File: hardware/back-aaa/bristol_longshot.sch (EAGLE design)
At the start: 7 parts, among them U4 ADP1607ACPZN-R7

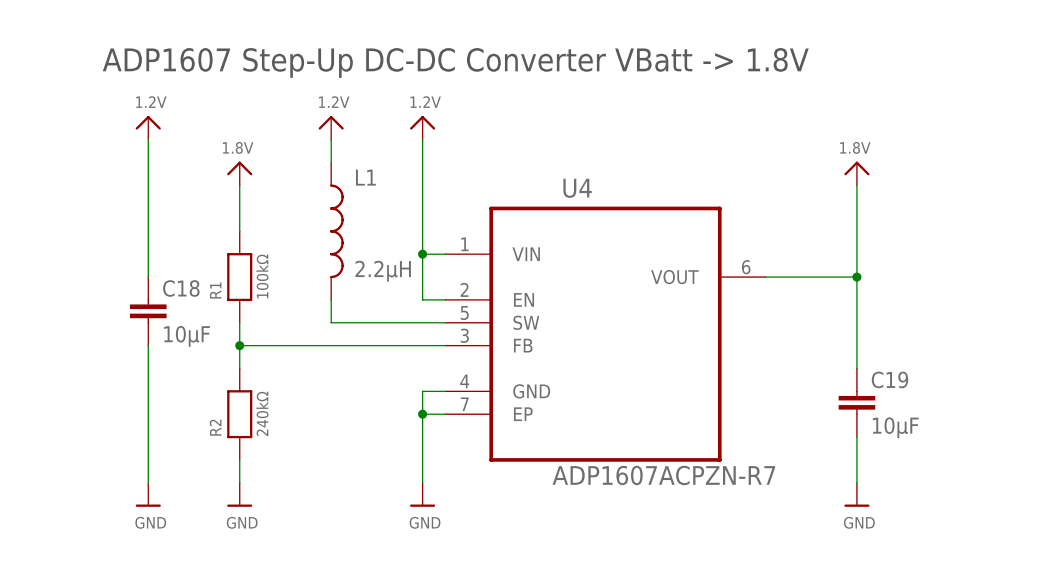
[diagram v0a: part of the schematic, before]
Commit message: Added partslist, updated parts for back-aaa
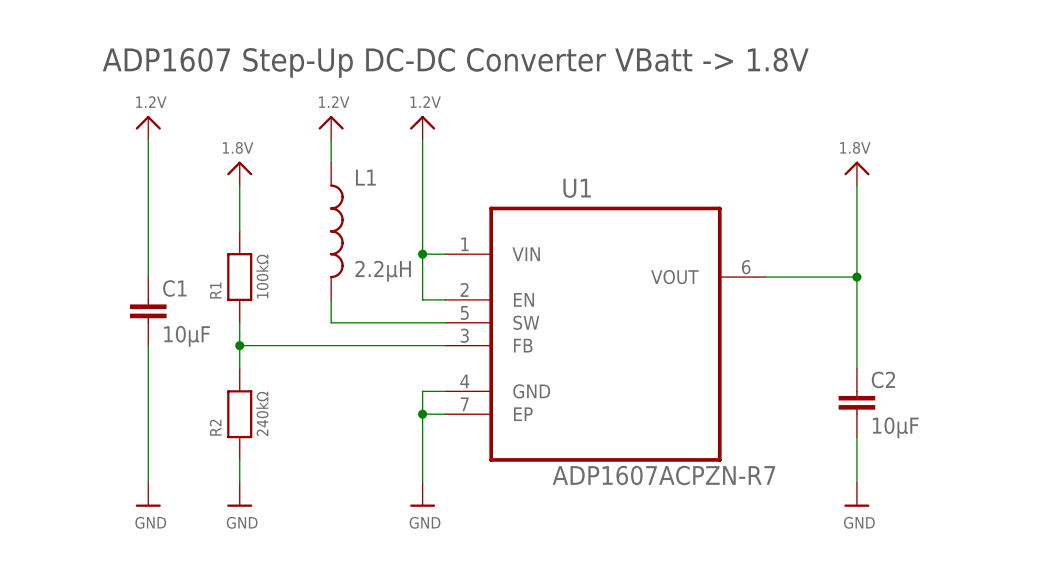
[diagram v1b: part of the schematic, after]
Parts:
- renumbered C18 to C1, C19 to C2, U4 to U1
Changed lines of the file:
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@@
 <part name="U$47" library="microbuilder_v3" deviceset="1.2V" device=""/>
 <part name="U$2" library="fbri" deviceset="AA_HOLDER" device=""/>
-<part name="C19" library="resistor" deviceset="C-EU" device="C0603K" value="10µF"/>
-<part name="U4" library="ADP1607" deviceset="ADP1607ACPZN-R7" device=""/>
+<part name="C2" library="resistor" deviceset="C-EU" device="C0603K" value="10µF"/>
+<part name="U1" library="ADP1607" deviceset="ADP1607ACPZN-R7" device=""/>
 <part name="U$26" library="microbuilder_v3" deviceset="1.2V" device=""/>
 <part name="R1" library="microbuilder_v3" deviceset="RESISTOR" device="_0402" value="100kΩ"/>
@@
 <part name="U$35" library="microbuilder_v3" deviceset="1.2V" device=""/>
 <part name="U$36" library="microbuilder_v3" deviceset="GND" device=""/>
-<part name="C18" library="resistor" deviceset="C-EU" device="C0603K" value="10µF"/>
+<part name="C1" library="resistor" deviceset="C-EU" device="C0603K" value="10µF"/>
 <part name="U$52" library="microbuilder_v3" deviceset="1.8V" device=""/>
 </parts>
@@
 <instance part="U$47" gate="G$1" x="60.96" y="106.68"/>
 <instance part="U$2" gate="G$1" x="60.96" y="86.36" rot="R270"/>
-<instance part="C19" gate="G$1" x="170.18" y="83.82"/>
-<instance part="U4" gate="A" x="142.24" y="93.98"/>
+<instance part="C2" gate="G$1" x="170.18" y="83.82"/>
+<instance part="U1" gate="A" x="142.24" y="93.98"/>
 <instance part="U$26" gate="G$1" x="111.76" y="114.3"/>
 <instance part="R1" gate="G$1" x="101.6" y="96.52" rot="R90"/>
@@
 <instance part="U$35" gate="G$1" x="91.44" y="114.3"/>
 <instance part="U$36" gate="G$1" x="91.44" y="71.12"/>
-<instance part="C18" gate="G$1" x="91.44" y="93.98"/>
+<instance part="C1" gate="G$1" x="91.44" y="93.98"/>
 <instance part="U$52" gate="G$1" x="101.6" y="109.22" rot="MR0"/>
 </instances>
@@
 <segment>
 <pinref part="U$29" gate="G$1" pin="GND"/>
-<pinref part="C19" gate="G$1" pin="2"/>
+<pinref part="C2" gate="G$1" pin="2"/>
 <wire x1="170.18" y1="73.66" x2="170.18" y2="78.74" width="0.1524" layer="91"/>
 </segment>
@@
 </segment>
 <segment>
-<pinref part="U4" gate="A" pin="GND"/>
+<pinref part="U1" gate="A" pin="GND"/>
 <pinref part="U$1" gate="G$1" pin="GND"/>
 <wire x1="124.46" y1="83.82" x2="121.92" y2="83.82" width="0.1524" layer="91"/>
 <wire x1="121.92" y1="83.82" x2="121.92" y2="81.28" width="0.1524" layer="91"/>
-<pinref part="U4" gate="A" pin="EP"/>
+<pinref part="U1" gate="A" pin="EP"/>
 <wire x1="121.92" y1="81.28" x2="121.92" y2="73.66" width="0.1524" layer="91"/>
 <wire x1="124.46" y1="81.28" x2="121.92" y2="81.28" width="0.1524" layer="91"/>
@@
 <segment>
 <pinref part="U$36" gate="G$1" pin="GND"/>
-<pinref part="C18" gate="G$1" pin="2"/>
+<pinref part="C1" gate="G$1" pin="2"/>
 <wire x1="91.44" y1="73.66" x2="91.44" y2="88.9" width="0.1524" layer="91"/>
 </segment>
@@
 <pinref part="U$30" gate="G$1" pin="1.8V"/>
 <wire x1="170.18" y1="86.36" x2="170.18" y2="96.52" width="0.1524" layer="91"/>
-<pinref part="C19" gate="G$1" pin="1"/>
-<pinref part="U4" gate="A" pin="VOUT"/>
+<pinref part="C2" gate="G$1" pin="1"/>
+<pinref part="U1" gate="A" pin="VOUT"/>
 <wire x1="170.18" y1="96.52" x2="170.18" y2="106.68" width="0.1524" layer="91"/>
 <wire x1="160.02" y1="96.52" x2="170.18" y2="96.52" width="0.1524" layer="91"/>
@@
 </segment>
 <segment>
-<pinref part="U4" gate="A" pin="VIN"/>
+<pinref part="U1" gate="A" pin="VIN"/>
 <pinref part="U$33" gate="G$1" pin="1.2V"/>
 <wire x1="124.46" y1="99.06" x2="121.92" y2="99.06" width="0.1524" layer="91"/>
 <wire x1="121.92" y1="99.06" x2="121.92" y2="111.76" width="0.1524" layer="91"/>
-<pinref part="U4" gate="A" pin="EN"/>
+<pinref part="U1" gate="A" pin="EN"/>
 <wire x1="124.46" y1="93.98" x2="121.92" y2="93.98" width="0.1524" layer="91"/>
 <wire x1="121.92" y1="93.98" x2="121.92" y2="99.06" width="0.1524" layer="91"/>
@@
 <pinref part="U$35" gate="G$1" pin="1.2V"/>
 <wire x1="91.44" y1="96.52" x2="91.44" y2="111.76" width="0.1524" layer="91"/>
-<pinref part="C18" gate="G$1" pin="1"/>
+<pinref part="C1" gate="G$1" pin="1"/>
 </segment>
 </net>
 <net name="SW" class="0">
 <segment>
-<pinref part="U4" gate="A" pin="SW"/>
+<pinref part="U1" gate="A" pin="SW"/>
 <wire x1="124.46" y1="91.44" x2="111.76" y2="91.44" width="0.1524" layer="91"/>
 <pinref part="L1" gate="G$1" pin="2"/>
@@
 <net name="FB" class="0">
 <segment>
-<pinref part="U4" gate="A" pin="FB"/>
+<pinref part="U1" gate="A" pin="FB"/>
 <pinref part="R2" gate="G$1" pin="2"/>
 <wire x1="124.46" y1="88.9" x2="101.6" y2="88.9" width="0.1524" layer="91"/>

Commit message: aaa-board mostly done
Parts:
- added C3: 100pF, microbuilder_v3:CAP_CERAMIC_0402
- added U$12: M04X2, fbri:M04X2
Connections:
- net 1.2V: now also U$12.5, U$2.+2; no longer U$2.+
- net 1.8V: now also C3.P$1, U$12.3
- net GND: now also C3.P$2, U$12.1, U$12.2, U$12.4, U$12.6
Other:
- note added: "GND, GND, 1.8V, Vbattery, DATA"
- note added: "NC, GND, Status, Vsolar, CLK"
- moved on the sheet: C2
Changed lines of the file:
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@@
 <part name="C1" library="resistor" deviceset="C-EU" device="C0603K" value="10µF"/>
 <part name="U$52" library="microbuilder_v3" deviceset="1.8V" device=""/>
+<part name="C3" library="microbuilder_v3" deviceset="CAP_CERAMIC" device="_0402" value="100pF"/>
+<part name="U$3" library="microbuilder_v3" deviceset="GND" device=""/>
+<part name="U$10" library="microbuilder_v3" deviceset="1.8V" device=""/>
+<part name="U$11" library="microbuilder_v3" deviceset="1.2V" device=""/>
+<part name="U$12" library="fbri" deviceset="M04X2" device=""/>
+<part name="U$6" library="microbuilder_v3" deviceset="GND" device=""/>
+<part name="U$13" library="microbuilder_v3" deviceset="GND" device=""/>
+<part name="U$14" library="microbuilder_v3" deviceset="GND" device=""/>
+<part name="U$15" library="microbuilder_v3" deviceset="GND" device=""/>
 </parts>
 <sheets>
@@
 connection on the
 holder</text>
+<text x="33.02" y="43.18" size="1.27" layer="97" font="vector" ratio="11">NC, GND, Status, Vsolar, CLK</text>
+<text x="33.02" y="5.08" size="1.27" layer="97" font="vector" ratio="11">GND, GND, 1.8V, Vbattery, DATA</text>
 </plain>
 <instances>
@@
 <instance part="FRAME1" gate="G$2" x="147.32" y="0"/>
 <instance part="U$1" gate="G$1" x="121.92" y="71.12"/>
-<instance part="U$29" gate="G$1" x="170.18" y="71.12"/>
-<instance part="U$30" gate="G$1" x="170.18" y="109.22" rot="MR0"/>
+<instance part="U$29" gate="G$1" x="185.42" y="71.12"/>
+<instance part="U$30" gate="G$1" x="185.42" y="109.22" rot="MR0"/>
 <instance part="L1" gate="G$1" x="111.76" y="101.6"/>
 <instance part="U$33" gate="G$1" x="121.92" y="114.3"/>
 <instance part="U$46" gate="G$1" x="60.96" y="71.12"/>
-<instance part="U$47" gate="G$1" x="60.96" y="106.68"/>
+<instance part="U$47" gate="G$1" x="63.5" y="106.68"/>
 <instance part="U$2" gate="G$1" x="60.96" y="86.36" rot="R270"/>
-<instance part="C2" gate="G$1" x="170.18" y="83.82"/>
+<instance part="C2" gate="G$1" x="185.42" y="83.82"/>
 <instance part="U1" gate="A" x="142.24" y="93.98"/>
 <instance part="U$26" gate="G$1" x="111.76" y="114.3"/>
@@
 <instance part="C1" gate="G$1" x="91.44" y="93.98"/>
 <instance part="U$52" gate="G$1" x="101.6" y="109.22" rot="MR0"/>
+<instance part="C3" gate="G$1" x="172.72" y="81.28"/>
+<instance part="U$3" gate="G$1" x="172.72" y="71.12"/>
+<instance part="U$10" gate="G$1" x="45.72" y="12.7" rot="MR180"/>
+<instance part="U$11" gate="G$1" x="48.26" y="12.7" rot="R180"/>
+<instance part="U$12" gate="G$1" x="48.26" y="27.94" rot="R90"/>
+<instance part="U$6" gate="G$1" x="43.18" y="17.78"/>
+<instance part="U$13" gate="G$1" x="43.18" y="38.1" rot="R180"/>
+<instance part="U$14" gate="G$1" x="45.72" y="38.1" rot="R180"/>
+<instance part="U$15" gate="G$1" x="48.26" y="38.1" rot="R180"/>
 </instances>
 <busses>
@@
 <pinref part="U$29" gate="G$1" pin="GND"/>
 <pinref part="C2" gate="G$1" pin="2"/>
-<wire x1="170.18" y1="73.66" x2="170.18" y2="78.74" width="0.1524" layer="91"/>
+<wire x1="185.42" y1="73.66" x2="185.42" y2="78.74" width="0.1524" layer="91"/>
 </segment>
 <segment>
@@
 <wire x1="91.44" y1="73.66" x2="91.44" y2="88.9" width="0.1524" layer="91"/>
 </segment>
+<segment>
+<pinref part="U$3" gate="G$1" pin="GND"/>
+<pinref part="C3" gate="G$1" pin="P$2"/>
+<wire x1="172.72" y1="73.66" x2="172.72" y2="78.74" width="0.1524" layer="91"/>
+</segment>
+<segment>
+<pinref part="U$12" gate="G$1" pin="1"/>
+<pinref part="U$6" gate="G$1" pin="GND"/>
+</segment>
+<segment>
+<pinref part="U$12" gate="G$1" pin="2"/>
+<pinref part="U$13" gate="G$1" pin="GND"/>
+</segment>
+<segment>
+<pinref part="U$12" gate="G$1" pin="4"/>
+<pinref part="U$14" gate="G$1" pin="GND"/>
+</segment>
+<segment>
+<pinref part="U$12" gate="G$1" pin="6"/>
+<pinref part="U$15" gate="G$1" pin="GND"/>
+</segment>
 </net>
 <net name="1.8V" class="0">
 <segment>
 <pinref part="U$30" gate="G$1" pin="1.8V"/>
-<wire x1="170.18" y1="86.36" x2="170.18" y2="96.52" width="0.1524" layer="91"/>
+<wire x1="185.42" y1="86.36" x2="185.42" y2="96.52" width="0.1524" layer="91"/>
 <pinref part="C2" gate="G$1" pin="1"/>
 <pinref part="U1" gate="A" pin="VOUT"/>
-<wire x1="170.18" y1="96.52" x2="170.18" y2="106.68" width="0.1524" layer="91"/>
-<wire x1="160.02" y1="96.52" x2="170.18" y2="96.52" width="0.1524" layer="91"/>
-<junction x="170.18" y="96.52"/>
+<wire x1="185.42" y1="96.52" x2="185.42" y2="106.68" width="0.1524" layer="91"/>
+<wire x1="160.02" y1="96.52" x2="172.72" y2="96.52" width="0.1524" layer="91"/>
+<junction x="185.42" y="96.52"/>
+<pinref part="C3" gate="G$1" pin="P$1"/>
+<wire x1="172.72" y1="96.52" x2="185.42" y2="96.52" width="0.1524" layer="91"/>
+<wire x1="172.72" y1="86.36" x2="172.72" y2="96.52" width="0.1524" layer="91"/>
+<junction x="172.72" y="96.52"/>
 </segment>
 <segment>
@@
 <wire x1="101.6" y1="101.6" x2="101.6" y2="106.68" width="0.1524" layer="91"/>
 </segment>
+<segment>
+<pinref part="U$10" gate="G$1" pin="1.8V"/>
+<pinref part="U$12" gate="G$1" pin="3"/>
+<wire x1="45.72" y1="15.24" x2="45.72" y2="20.32" width="0.1524" layer="91"/>
+</segment>
 </net>
 <net name="1.2V" class="0">
-<segment>
-<pinref part="U$47" gate="G$1" pin="1.2V"/>
-<wire x1="60.96" y1="90.17" x2="60.96" y2="104.14" width="0.1524" layer="91"/>
-<pinref part="U$2" gate="G$1" pin="+"/>
-</segment>
 <segment>
 <pinref part="U1" gate="A" pin="VIN"/>
@@
 <pinref part="C1" gate="G$1" pin="1"/>
 </segment>
+<segment>
+<pinref part="U$2" gate="G$1" pin="+2"/>
+<pinref part="U$47" gate="G$1" pin="1.2V"/>
+<wire x1="63.5" y1="91.44" x2="63.5" y2="104.14" width="0.1524" layer="91"/>
+</segment>
+<segment>
+<pinref part="U$11" gate="G$1" pin="1.2V"/>
+<pinref part="U$12" gate="G$1" pin="5"/>
+<wire x1="48.26" y1="15.24" x2="48.26" y2="20.32" width="0.1524" layer="91"/>
+</segment>
 </net>
